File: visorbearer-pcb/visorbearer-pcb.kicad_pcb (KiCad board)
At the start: 2 copper layers, 224 x 98.5 mm, 81 parts, among them U1 XIAO nRF52840 Plus, U3 LP5012, U5 LP5012

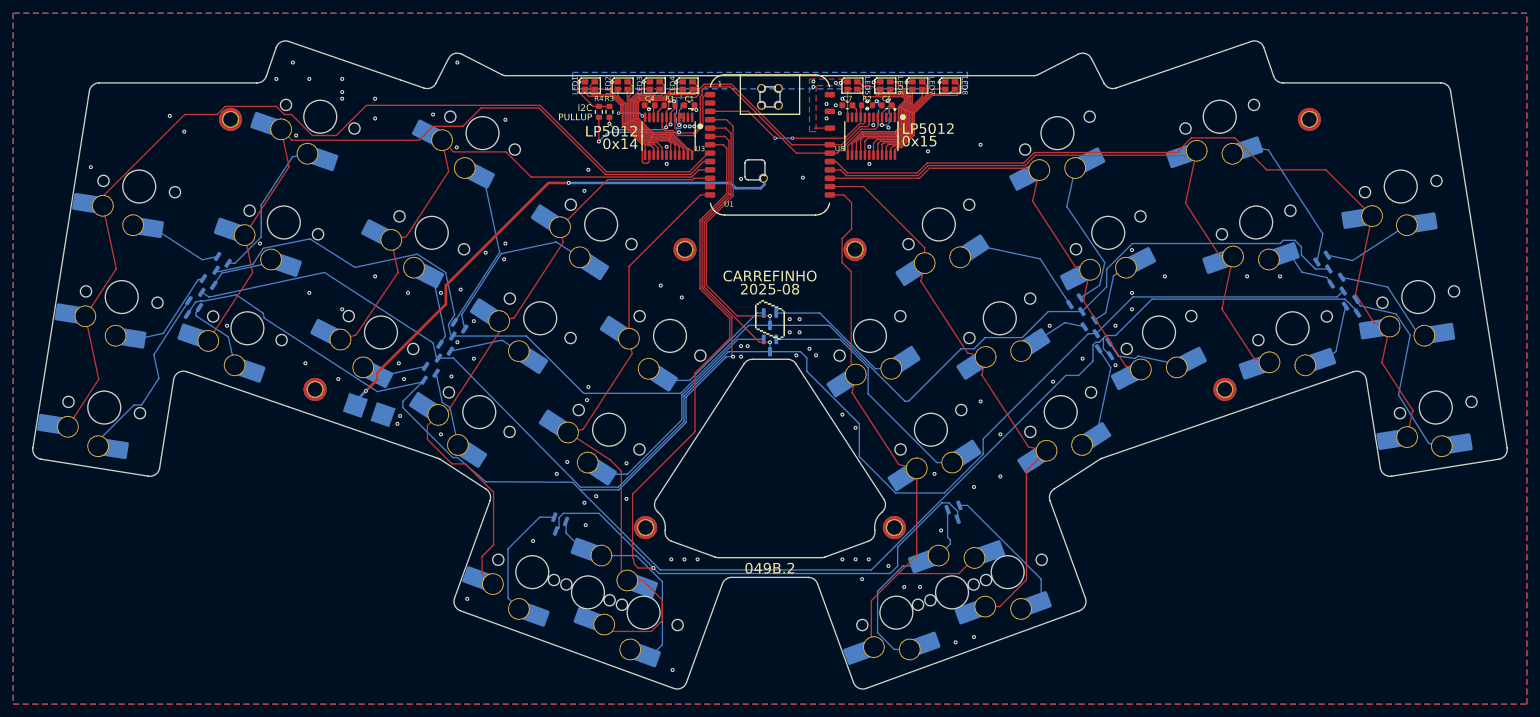
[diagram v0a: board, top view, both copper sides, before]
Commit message: pcb: change to hand-solderable diode footprint, move battery pads, add LP5012 EN test points
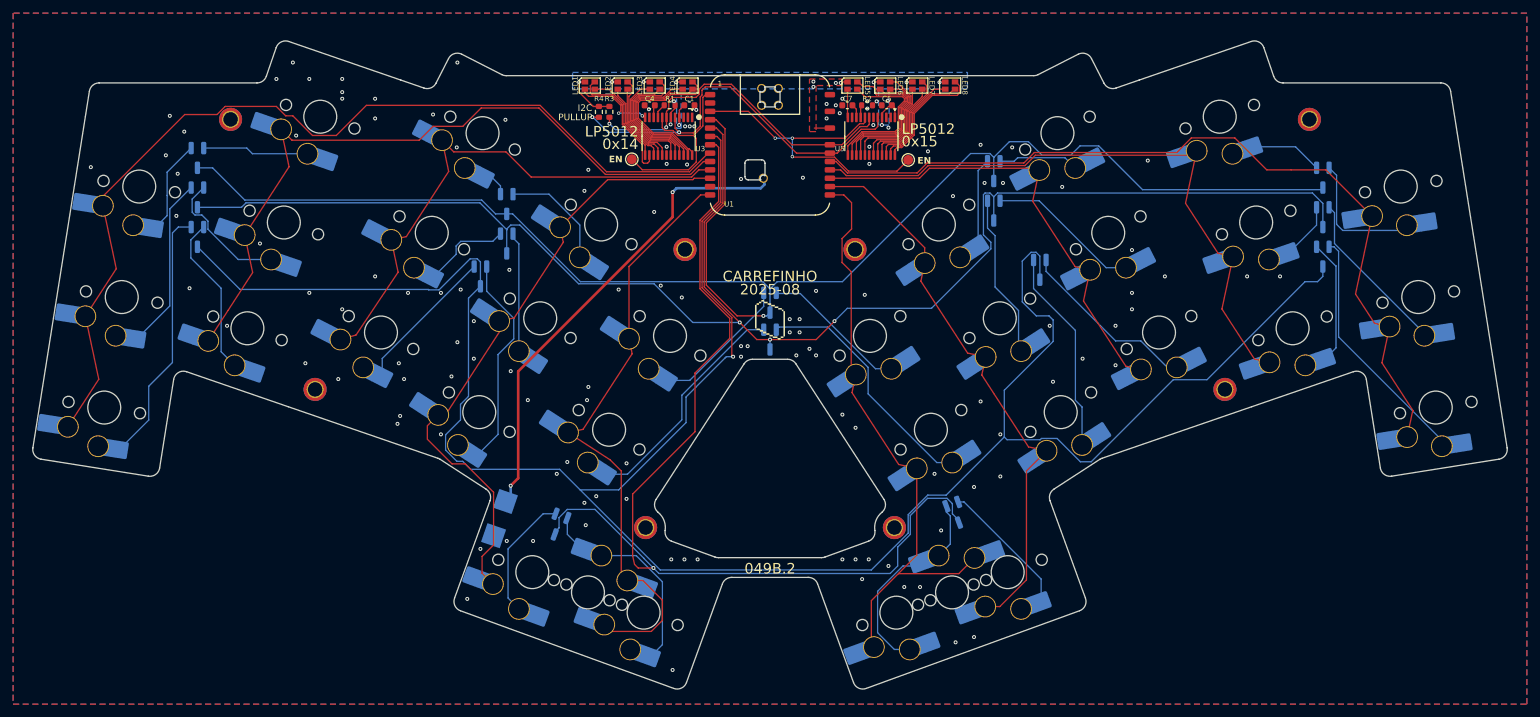
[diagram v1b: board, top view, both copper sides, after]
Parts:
- added TP3: LPA_EN, TestPoint:TestPoint_Pad_D1.5mm, F.Cu at (-21.0, 2.20)
- added TP4: LPB_EN, TestPoint:TestPoint_Pad_D1.5mm, F.Cu at (21.0, 2.30)
- D1, D10, D11, D12, D13, D14, D15, D16, D2, D3, D4, D5, D6, D7, D8, D9: footprint Package_TO_SOT_SMD:SOT-23 -> Package_TO_SOT_SMD:SOT-23_Handsoldering
- TP1: value TestPoint -> BAT+
- TP2: value TestPoint -> BAT-
- moved TP1 27.1 mm to (-40.2, 54.2)
- moved TP2 24.9 mm to (-42.0, 59.4)
- moved D4 24.3 mm to (34.0, 4.00), turned to -90 degrees
- moved D9 23.4 mm to (34.0, 10.0), turned to -90 degrees
- moved D2 20.7 mm to (-40.0, 9.00), turned to -90 degrees
- moved D7 19.3 mm to (-40.0, 15.0), turned to -90 degrees
- moved D12 17.0 mm to (-44.0, 20.0), turned to -90 degrees
- moved D1 16.6 mm to (-87.0, 2.00), turned to -90 degrees
- moved D13 16.0 mm to (41.0, 19.0), turned to -90 degrees
- moved D6 13.7 mm to (-87.0, 8.00), turned to -90 degrees
- moved D5 13.1 mm to (84.0, 5.00), turned to -90 degrees
- moved D11 11.0 mm to (-87.0, 14.0), turned to -90 degrees
- moved D10 10.7 mm to (84.0, 11.0), turned to -90 degrees
- moved D14 9.13 mm to (84.0, 17.0), turned to -90 degrees
- moved D3 2.50 mm to (0.00, 24.0)
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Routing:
- net /ROW2: track 298.4 -> 355.6 mm
- net /ROW1: track 268.0 -> 243.4 mm, vias 1 -> 3
- net /LPB_EN: track 26.5 -> 48.5 mm, vias 2 -> 3
- net Net-(CH24-Pad2): track 11.8 -> 33.0 mm
- net Net-(CH3-Pad2): track 24.3 -> 4.30 mm
- net Net-(CH25-Pad2): track 13.7 -> 31.2 mm
- net Net-(CH17-Pad2): track 7.70 -> 25.0 mm
- net Net-(CH23-Pad2): track 6.87 -> 22.6 mm
- net Net-(CH26-Pad2): track 12.0 -> 27.6 mm
- net /LPA_EN: track 15.0 -> 30.1 mm
- net Net-(CH18-Pad2): track 9.99 -> 23.4 mm
- net Net-(CH22-Pad2): track 11.7 -> 24.6 mm
- net /ROW0: track 251.4 -> 239.5 mm
- net Net-(CH11-Pad2): track 14.7 -> 26.4 mm
- net Net-(CH21-Pad2): track 28.0 -> 39.5 mm
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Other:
- board text added: "EN"

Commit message: add standard case files & update pcb
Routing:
- net /SDA: track 61.1 -> 62.9 mm
- net /LPB_EN: track 48.5 -> 46.7 mm
- net GND: vias 137 -> 106

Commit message: add ergogen files
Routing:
- net GND: vias 106 -> 99
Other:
- board text added: "github.com/carrrefinho/visorbearer"
